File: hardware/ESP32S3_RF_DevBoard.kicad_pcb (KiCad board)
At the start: 2 copper layers, 37 parts, among them J1 USB4105-GF-A, J2 Conn_01x22, J3 Conn_01x22, SW1 BOOT, SW2 RESET, U1 ESD122DMYR, U2 LD1117DT33CTR, U3 ESP32-S3-WROOM-1-N8, U4 SN74AHCT1G125DBVR

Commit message: - did board setup and constraints - did net classes - confirmed board outline and dimesions - placing U3 with the keepout area in mind heree
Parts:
- moved C2 231.1 mm to (353.0, 137.5)
- moved C6 231.1 mm to (353.0, 140.5)
- moved TP4 231.1 mm to (346.2, 136.9)
- moved C1 231.1 mm to (311.7, 127.5)
- moved C3 231.1 mm to (324.8, 138.5)
- moved C4 231.1 mm to (311.7, 130.0)
- moved C5 231.1 mm to (311.7, 132.5)
- moved C7 231.1 mm to (311.7, 135.0)
- moved C8 231.1 mm to (311.7, 137.5)
- moved D1 231.1 mm to (357.4, 140.4)
- moved D2 231.1 mm to (346.7, 139.7)
- moved J1 231.1 mm to (327.4, 132.9)
- moved J3 231.1 mm to (307.4, 86.3)
- moved R1 231.1 mm to (311.7, 140.0)
- moved R2 231.1 mm to (315.7, 127.5)
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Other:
- board outline added: 25.4 x 60 mm
- copper layers 2 -> 4

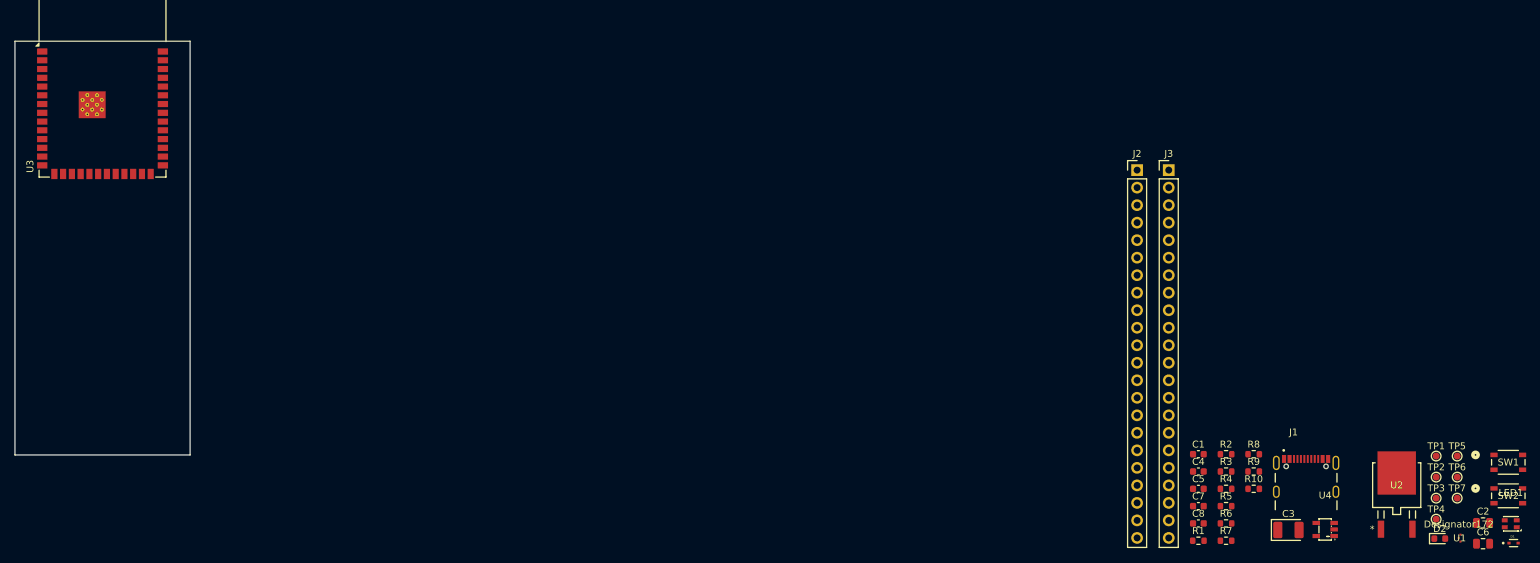
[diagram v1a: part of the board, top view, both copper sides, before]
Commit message: placement of all components and editing skilscreen rules
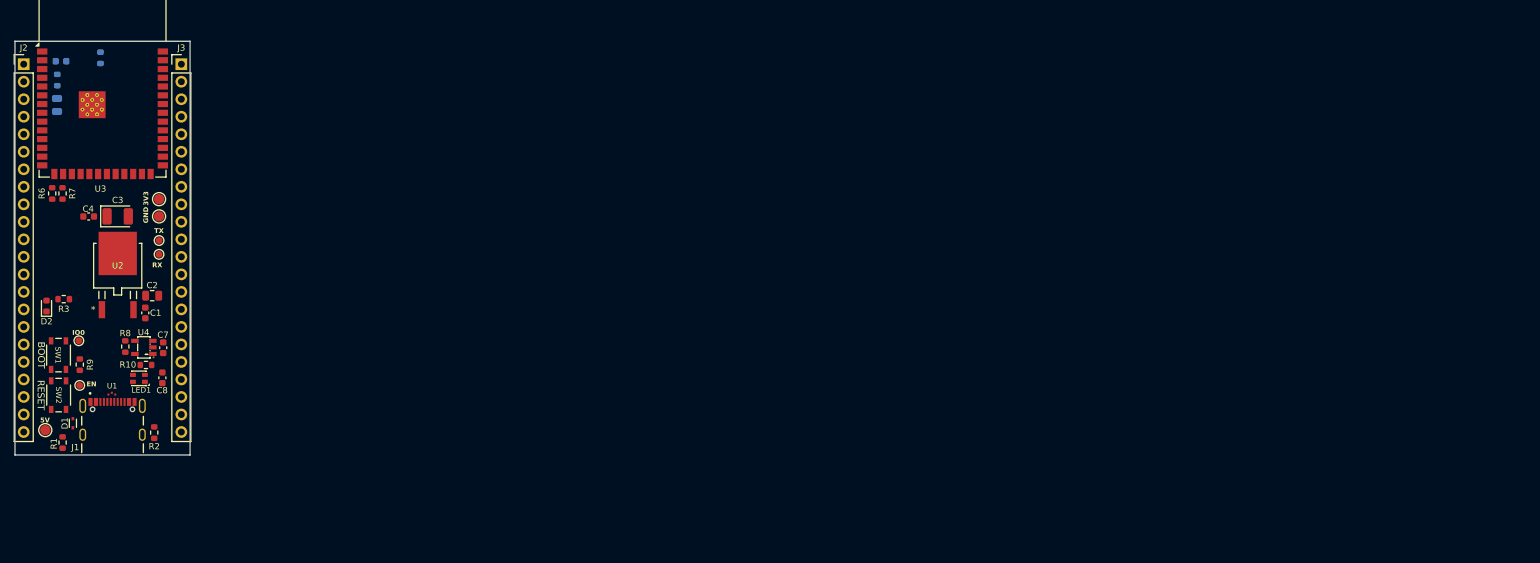
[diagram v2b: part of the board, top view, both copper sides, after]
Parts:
- C5, C6, R4, R5: moved to B.Cu
- TP1, TP2, TP3: footprint TestPoint:TestPoint_Pad_D1.0mm -> TestPoint:TestPoint_Pad_D1.5mm
- moved C6 216.4 mm to (146.2, 76.8), turned to -90 degrees
- moved SW1 210.8 mm to (146.4, 113.1), turned to -90 degrees
- moved SW2 210.7 mm to (146.4, 118.9), turned to -90 degrees
- moved D1 209.7 mm to (148.5, 123.0), turned to -90 degrees
- moved D2 204.9 mm to (144.7, 106.0), turned to 90 degrees
- moved TP1 201.7 mm to (144.5, 124.0)
- moved TP5 200.6 mm to (149.4, 111.0)
- moved LED1 200.1 mm to (158.1, 116.5)
- moved TP4 197.7 mm to (149.5, 117.5), turned to -90 degrees
- moved U1 196.6 mm to (154.2, 118.7), turned to -90 degrees
- moved C2 195.8 mm to (160.0, 104.5)
- moved TP7 191.6 mm to (161.0, 98.5)
- moved TP6 191.4 mm to (161.0, 96.5)
- moved TP3 189.7 mm to (161.0, 93.0)
- moved TP2 189.5 mm to (161.0, 90.5)
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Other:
- board text added: "3V3"
- board text added: "5V"
- board text added: "EN"
- board text added: "ESP32-S3 RF DEVBOARD REV v1 • 2026 Antoinette N Kellam"
- board text added: "GND"
- board text added: "IO0"
- board text added: "RX"
- board text added: "TX"

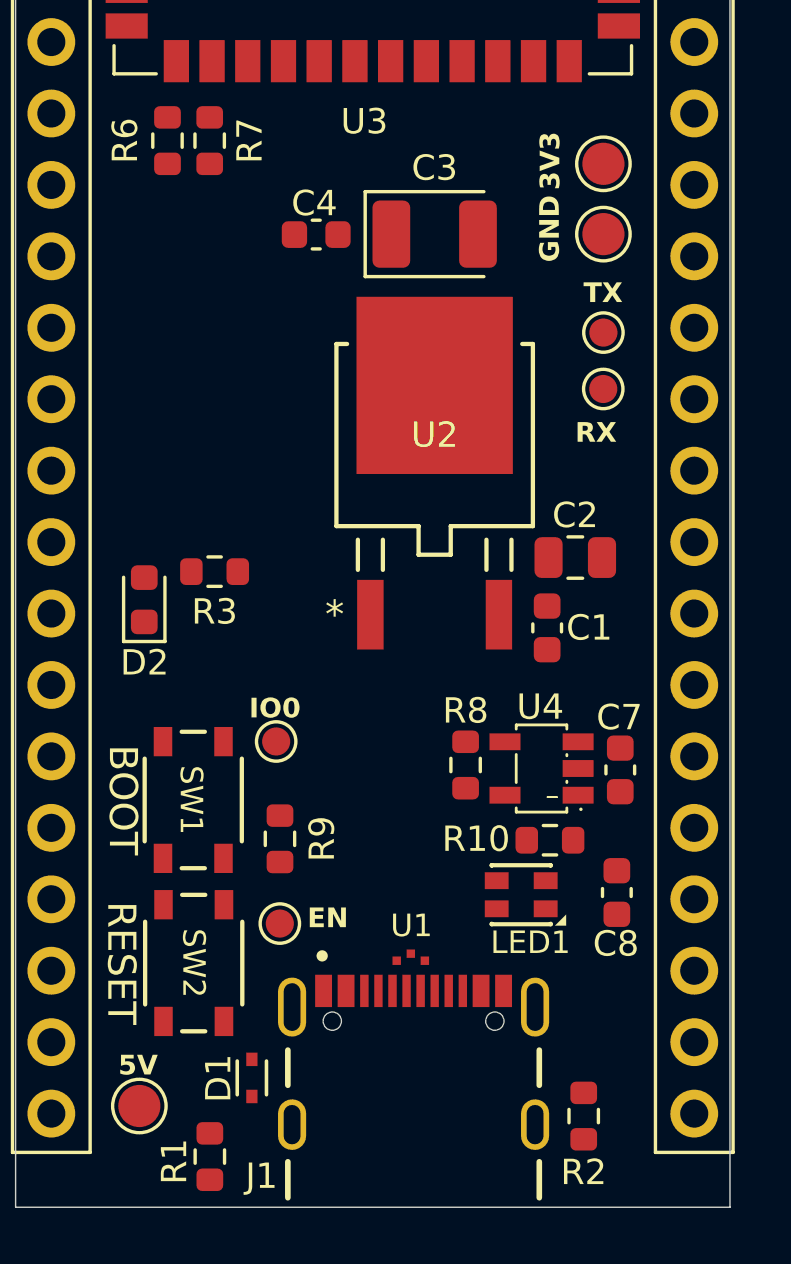
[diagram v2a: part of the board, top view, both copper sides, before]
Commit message: - made In.Cu GND plane - next: working on the routing USB.
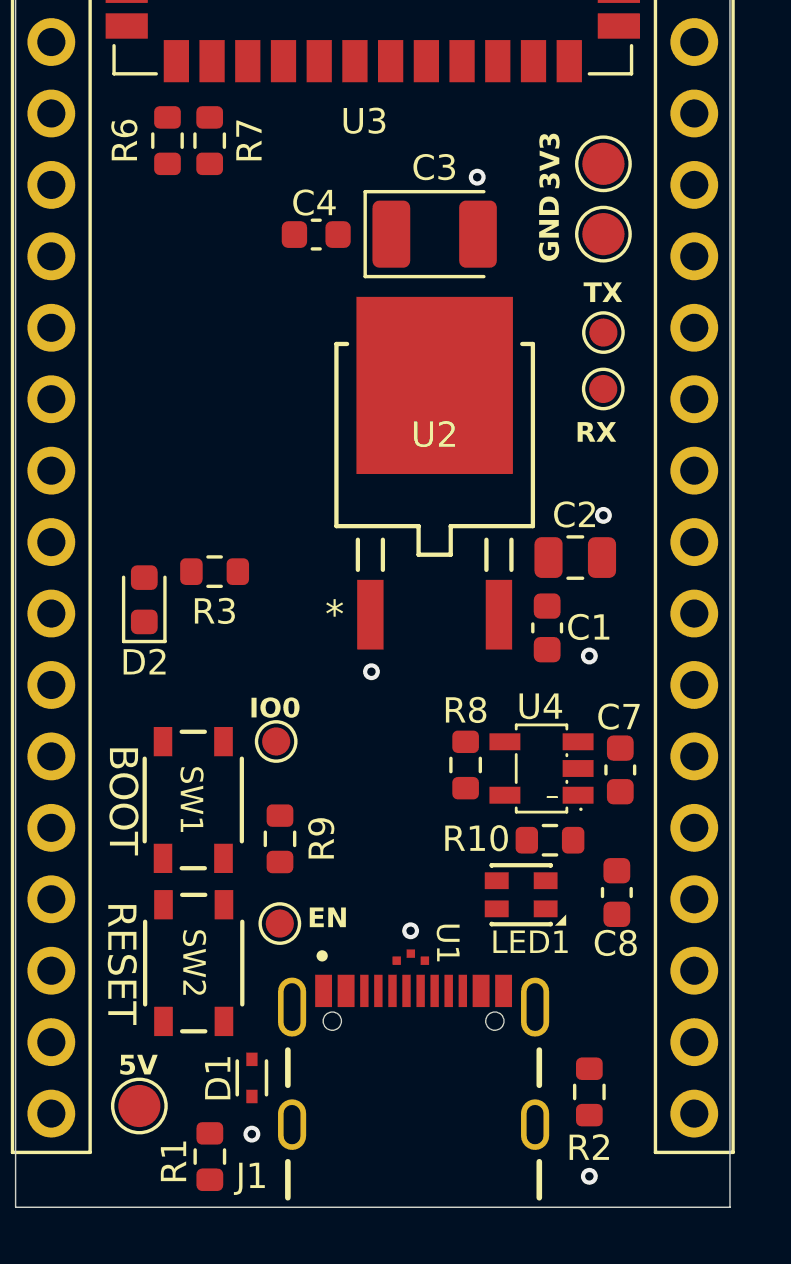
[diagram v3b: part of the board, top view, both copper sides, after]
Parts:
- moved R2 0.88 mm to (160.5, 123.5)
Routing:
- net GND: vias 0 -> 7
- added copper zone on In1.Cu, net GND
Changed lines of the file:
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@@
 				(material "1080 RC67%")
 				(epsilon_r 3.91)
-				(loss_tangent 0) addsublayer
+				(loss_tangent 0.02) addsublayer
 				(thickness 0.218)
 				(material "7628 RC49%")
 				(epsilon_r 4.4)
-				(loss_tangent 0)
+				(loss_tangent 0.02)
 			)
 			(layer "B.Cu"
@@
 		(at 154.25 124.6625)
 		(property "Reference" "J1"
-			(at -5.404653 1.831969 180)
+			(at -5.75 1.8375 180)
 			(layer "F.SilkS")
 			(effects
@@
 		)
 		(fp_text user "U1"
-			(at -1.118997 -0.024997 0)
+			(at -0.501237 -1.304723 270)
 			(unlocked yes)
 			(layer "F.SilkS")
@@
 	(footprint "Resistor_SMD:R_0603_1608Metric"
 		(layer "F.Cu")
-		(at 160.299029 124.358569 -90)
+		(at 160.5 123.5 -90)
 		(descr "Resistor SMD 0603 (1608 Metric), square (rectangular) end terminal, IPC-7351 nominal, (Body size source: IPC-SM-782 page 72, https://www.pcb-3d.com/wordpress/wp-content/uploads/ipc-sm-782a_amendment_1_and_2.pdf)")
 		(tags "resistor")
@@
 		)
 	)
+	(via
+		(at 148.5 125)
+		(size 0.6)
+		(drill 0.3)
+		(layers "F.Cu" "B.Cu")
+		(free yes)
+		(net "GND")
+	)
+	(via
+		(at 152.752544 108.559036)
+		(size 0.6)
+		(drill 0.3)
+		(layers "F.Cu" "B.Cu")
+		(free yes)
+		(net "GND")
+	)
+	(via
+		(at 160.5 108)
+		(size 0.6)
+		(drill 0.3)
+		(layers "F.Cu" "B.Cu")
+		(free yes)
+		(net "GND")
+	)
+	(via
+		(at 156.51297 90.975099)
+		(size 0.6)
+		(drill 0.3)
+		(layers "F.Cu" "B.Cu")
+		(free yes)
+		(net "GND")
+	)
+	(via
+		(at 154.145615 117.77036)
+		(size 0.6)
+		(drill 0.3)
+		(layers "F.Cu" "B.Cu")
+		(free yes)
+		(net "GND")
+	)
+	(via
+		(at 161 103)
+		(size 0.6)
+		(drill 0.3)
+		(layers "F.Cu" "B.Cu")
+		(free yes)
+		(net "GND")
+	)
+	(via
+		(at 160.5 126.5)
+		(size 0.6)
+		(drill 0.3)
+		(layers "F.Cu" "B.Cu")
+		(net "GND")
+	)
+	(zone
+		(net "GND")
+		(layer "In1.Cu")
+		(hatch edge 0.5)
+		(connect_pads
+			(clearance 0.2)
+		)
+		(min_thickness 0.25)
+		(fill yes
+			(thermal_gap 0.5)
+			(thermal_bridge_width 0.5)
+			(island_removal_mode 0)
+		)
+		(polygon
+			(pts
+				(xy 140 127.5) (xy 165.472643 127.591188) (xy 165.5 67.5) (xy 139.5 67.5)
+			)
+		)
+	)
